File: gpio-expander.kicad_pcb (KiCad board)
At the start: 2 copper layers, 29.2 x 29.4 mm, 13 parts, among them J1 Conn_01x06, J2 Conn_02x07_Odd_Even, J3 Conn_02x04_Odd_Even, U1 TCA9555DBT

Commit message: Rev 1.2
Signed-off-by: Aaron Williams <aaron.w2@gmail.com>
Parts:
- removed JP1, JP2, JP3: SolderJumper_2_Open, SolderJumper:SolderJumper-2_P1.3mm_Open_TrianglePad1.0x1.5mm
- added SW1: SW_DIP_x06, Buttons_Switches_SMD:SW_DIP_x6_W5.08mm_Slide_Copal_CHS-A, F.Cu at (146.2, 109.2)
- C1: footprint Capacitors_SMD:C_0603_HandSoldering -> Capacitor_SMD:C_0603_1608Metric
- C2, C3, C4: footprint Capacitors_SMD:C_0805_HandSoldering -> Capacitor_SMD:C_0805_2012Metric
- J1: footprint Connector_PinHeader_2.00mm:PinHeader_1x06_P2.00mm_Horizontal -> Pin_Headers:Pin_Header_Angled_1x06_Pitch2.54mm
- RN1, RN2: footprint Resistors_SMD:R_Array_Convex_4x0603 -> Resistor_SMD:R_Array_Convex_4x0603
- moved RN2 4.71 mm to (139.2, 110.6), turned to 270 degrees
- moved C3 1.98 mm to (138.7, 105.2), turned to 180 degrees
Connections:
- RN1 pad 5: +3V3 -> Net-(RN1-Pad5)
- RN1 pad 6: +3V3 -> Net-(RN1-Pad6)
- RN1 pad 7: +3V3 -> Net-(RN1-Pad7)
- RN1 pad 8: +3V3 -> Net-(RN1-Pad8)
- RN2 pad 1: +3V3 -> Net-(RN2-Pad1)
- RN2 pad 2: +3V3 -> /A0
- RN2 pad 3: +3V3 -> /A1
- RN2 pad 4: +3V3 -> /A2
- RN2 pad 5: Net-(RN2-Pad5) -> GND
- RN2 pad 6: /A2 -> GND
- RN2 pad 7: /A1 -> GND
- RN2 pad 8: /A0 -> Net-(RN2-Pad8)
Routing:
- net Net-(RN1-Pad6): track 0.00 -> 13.9 mm, vias 0 -> 2
- net Net-(RN1-Pad7): track 0.00 -> 13.7 mm, vias 0 -> 2
- net Net-(RN1-Pad8): track 0.00 -> 13.1 mm, vias 0 -> 2
- net /A0: track 13.0 -> 23.2 mm, vias 0 -> 2
- net /~INT: track 19.0 -> 27.9 mm, vias 2 -> 1
- net +3V3: track 12.3 -> 5.49 mm
- net /A2: track 24.4 -> 20.1 mm
- net /A1: track 22.0 -> 17.9 mm, vias 0 -> 2
- net GND: track 17.5 -> 14.9 mm, vias 6 -> 3
- net /SCL: track 11.5 -> 12.0 mm
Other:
- board text added: "1"
- board text added: "6"
- board text added: "I2C Address: 0x20-0x27"
- board text added: "Rev 1.2"
- board text added: "SW: 1: INT PU 2: SDA PU 3: SCL PU 4: A2 5: A1 6: A0"
- board text removed: "A0"
- board text removed: "A1"
- board text removed: "A2"

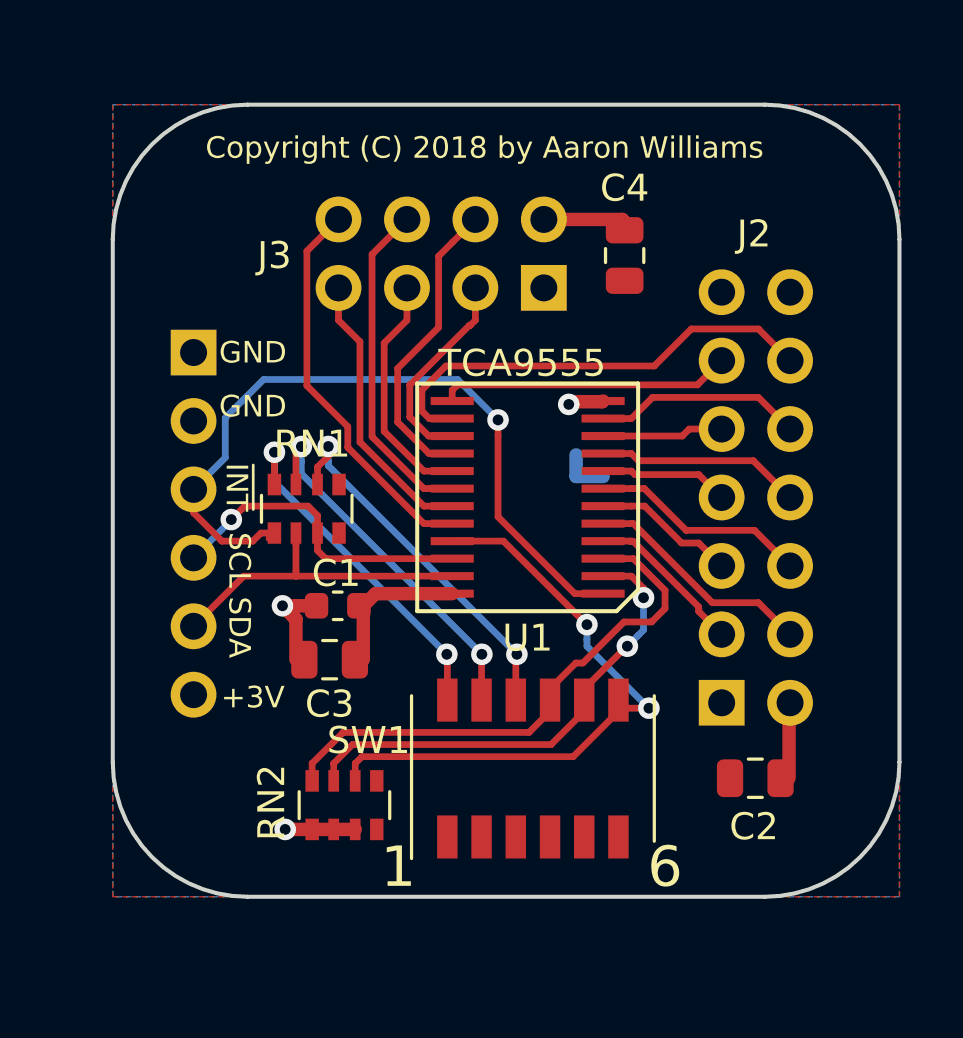
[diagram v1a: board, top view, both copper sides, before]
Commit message: - Added a dip switch for setting the address and termination - Added mounting holes - Changed J1 to a 10-pin connector with all pins duplicated   for stacking - Minor cleanup - Updated README
Signed-off-by: Aaron Williams <aaron.w2@gmail.com>
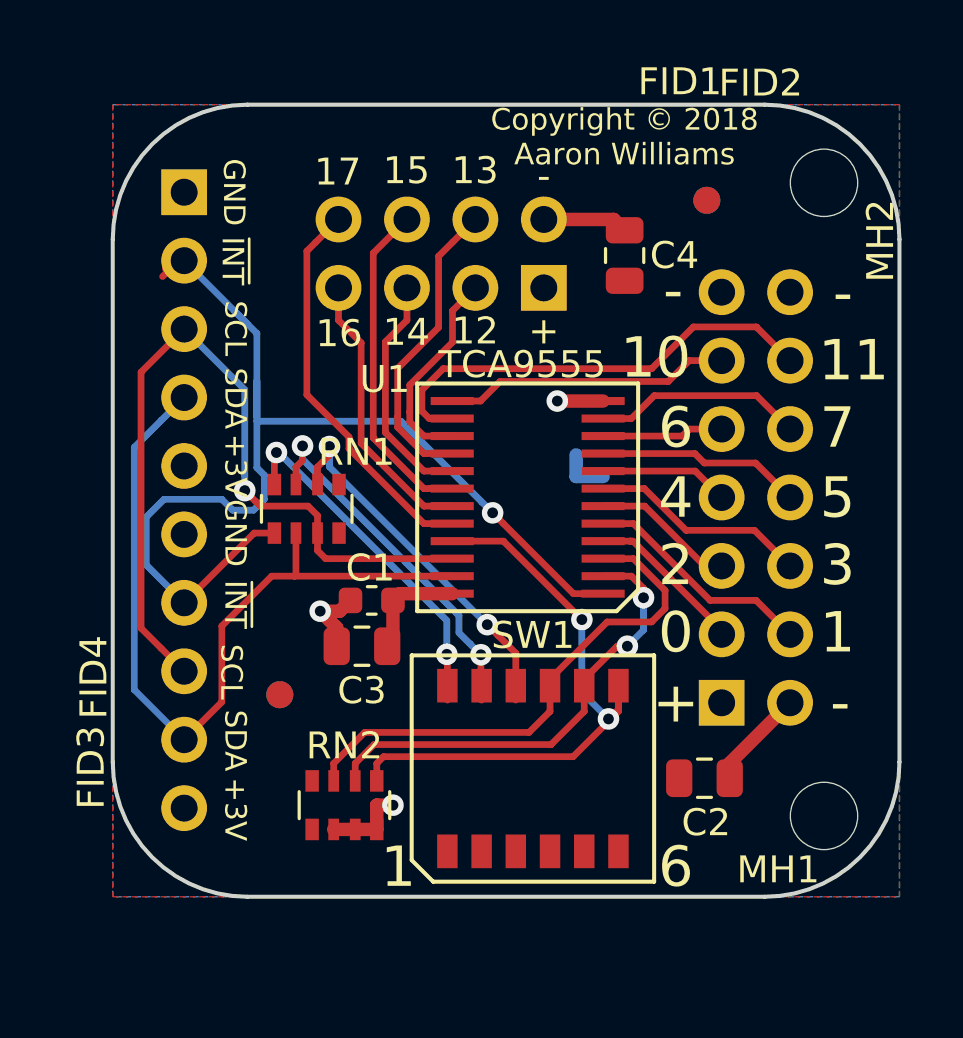
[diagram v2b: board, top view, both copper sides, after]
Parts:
- added FID1: FIDUCIAL_1MM, Fiducial:Fiducial_1mm_Dia_2.54mm_Outer_CopperTop, F.Cu at (152.7, 88.2)
- added FID2: FIDUCIAL_1MM, Fiducial:Fiducial_1mm_Dia_2.54mm_Outer_CopperBottom, F.Cu at (152.7, 88.2)
- added FID3: FIDUCIAL_1MM, Fiducial:Fiducial_1mm_Dia_2.54mm_Outer_CopperBottom, F.Cu at (136.8, 106.5)
- added FID4: FIDUCIAL_1MM, Fiducial:Fiducial_1mm_Dia_2.54mm_Outer_CopperTop, F.Cu at (136.8, 106.5)
- added MH1: MountingHole, MountingHole:MountingHole_2.5mm, F.Cu at (156.9, 111.0)
- added MH2: MountingHole, MountingHole:MountingHole_2.5mm, F.Cu at (157.0, 87.5)
- J1: value Conn_01x06 -> Conn_01x10; footprint Pin_Headers:Pin_Header_Angled_1x06_Pitch2.54mm -> Pin_Headers:Pin_Header_Angled_1x10_Pitch2.54mm
- SW1: footprint Buttons_Switches_SMD:SW_DIP_x6_W5.08mm_Slide_Copal_CHS-A -> Aaron:SW_DIP_SPSTx06_Slide_GrayHill_97C06_W4.5mm_P1.27mm
- moved J1 5.96 mm to (133.2, 87.8)
- moved C2 1.89 mm to (152.6, 109.6)
- moved C3 1.30 mm to (139.8, 104.7)
- moved C1 1.28 mm to (140.2, 103.0)
- turned SW1 to 0 degrees
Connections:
- net Net-(RN1-Pad6) renamed /SDA_PU
- net Net-(RN1-Pad7) renamed /SCL_PU
- net Net-(RN1-Pad8) renamed /~INT_PU
- J1 pad 2: GND -> /~INT
- J1 pad 3: /~INT -> /SCL
- J1 pad 4: /SCL -> /SDA
- J1 pad 5: /SDA -> +3V3
- J1 pad 6: +3V3 -> GND
- RN2 pad 1: Net-(RN2-Pad1) -> /A0
- RN2 pad 2: /A0 -> /A1
- RN2 pad 3: /A1 -> /A2
- RN2 pad 4: /A2 -> Net-(RN2-Pad4)
- RN2 pad 5: GND -> Net-(RN2-Pad5)
- RN2 pad 8: Net-(RN2-Pad8) -> GND
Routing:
- net /SCL: track 12.0 -> 30.5 mm
- net /SDA: track 12.4 -> 30.0 mm
- net /~INT: track 27.9 -> 43.3 mm
- net GND: track 14.9 -> 16.4 mm
- net +3V3: track 5.49 -> 4.09 mm
- net /A1: track 17.9 -> 17.4 mm
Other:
- board text added: "+"
- board text added: "-"
- board text added: "0"
- board text added: "10"
- board text added: "11"
- board text added: "12"
- board text added: "13"
- board text added: "14"
- board text added: "15"
- board text added: "16"
- board text added: "17"
- board text added: "2"
- board text added: "3"
- board text added: "4"
- board text added: "5"
- board text added: "7"
- board text added: "Copyright © 2018 Aaron Williams"
- board text removed: "Copyright (C) 2018 by Aaron Williams"

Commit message: Fixed solder mask clearance.
Signed-off-by: Aaron Williams <aaron.w2@gmail.com>
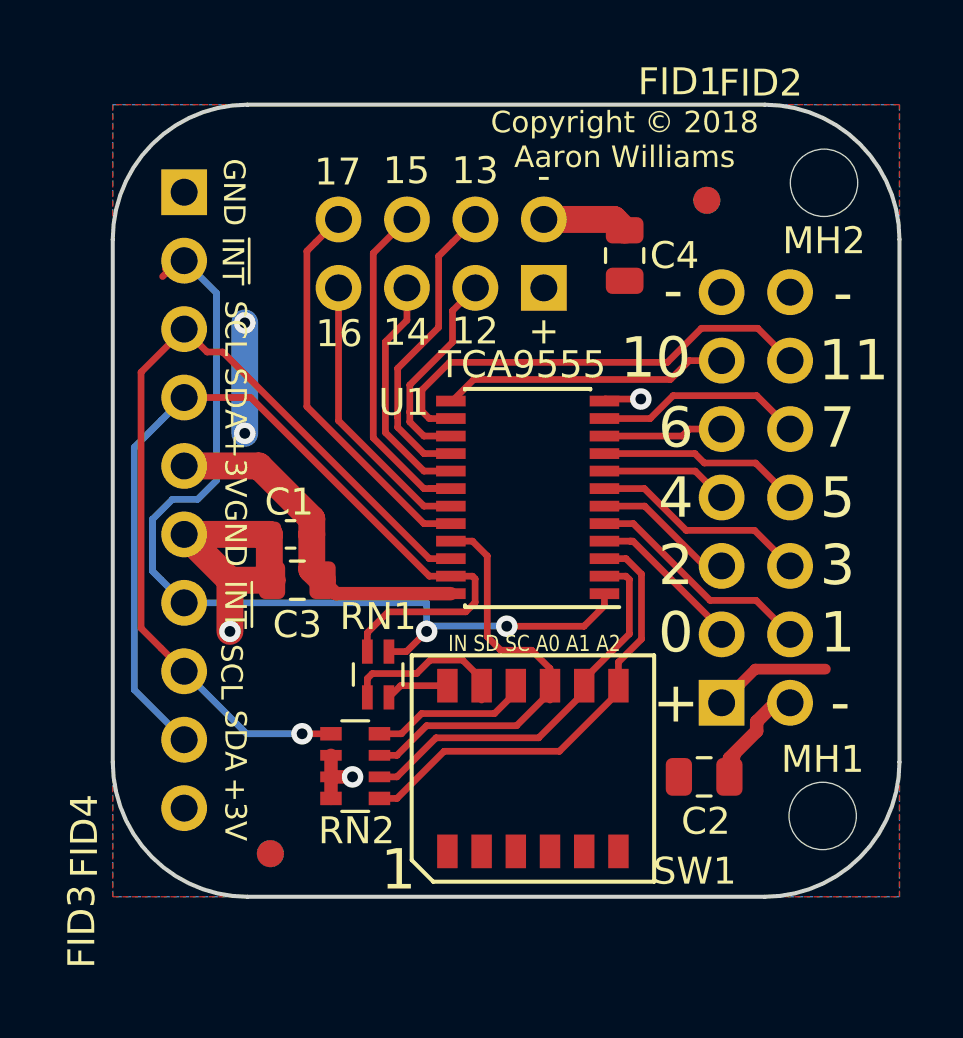
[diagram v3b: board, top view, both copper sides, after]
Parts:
- RN1: value 10k -> R_Pack02; footprint Resistor_SMD:R_Array_Convex_4x0603 -> Resistor_SMD:R_Array_Concave_2x0603
- U1: footprint Housings_SSOP:SOIC-24_5.3x6.2mm_Pitch0.65 -> Housings_SSOP:TSSOP-24_4.4x7.8mm_Pitch0.65mm
- moved RN1 6.70 mm to (140.4, 105.8), turned to 270 degrees
- moved FID3 5.91 mm to (136.4, 112.4)
- moved FID4 5.91 mm to (136.4, 112.4)
- moved C1 3.88 mm to (137.2, 100.5)
- moved C3 3.43 mm to (137.4, 102.2)
- moved RN2 1.50 mm to (139.6, 109.2), turned to 180 degrees
- moved C2 0.05 mm to (152.6, 109.5)
- turned U1 to 180 degrees
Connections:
- RN1 pad 3: /SCL -> /SDA_PU
- RN1 pad 4: Net-(RN1-Pad4) -> /~INT_PU
- RN2 pad 1: /A0 -> /A2
- RN2 pad 3: /A2 -> /A0
- RN2 pad 4: Net-(RN2-Pad4) -> /SCL_PU
- RN2 pad 5: Net-(RN2-Pad5) -> /SCL
- SW1 pad 10: /SDA_PU -> /SCL_PU
- SW1 pad 11: /SCL_PU -> /SDA_PU
- SW1 pad 7: /A0 -> /A2
- SW1 pad 9: /A2 -> /A0
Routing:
- net +3V3: track 4.09 -> 21.4 mm, vias 0 -> 2
- net /~INT_PU: track 13.1 -> 2.35 mm, vias 2 -> 0
- net /SDA_PU: track 13.9 -> 5.80 mm, vias 2 -> 0
- net /SCL_PU: track 13.7 -> 5.94 mm, vias 2 -> 0
- net /A0: track 22.9 -> 16.2 mm, vias 2 -> 0
- net /~INT: track 43.3 -> 36.8 mm, vias 1 -> 2
- net GND: track 16.4 -> 22.1 mm
- net /SDA: track 30.0 -> 33.9 mm
- net /SCL: track 30.5 -> 33.9 mm
- net /A2: track 19.9 -> 16.9 mm
- net /A1: track 17.4 -> 14.8 mm, vias 2 -> 0
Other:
- rule pad_to_mask_clearance: 0.2 -> 0.0508
- board text added: "1.65-6V I2C GPIO Expander"
- board text added: "IN SD SC A0 A1 A2"
- board text added: "Rev 1.3"
- board text added: "Switch SW1: 1: INT PU 2: SDA PU 3: SCL PU 4: A0 5: A1 6: A2"
- board text removed: "3V I2C GPIO Expander"
- board text removed: "Rev 1.2"
- board text removed: "SW: 1: INT PU 2: SDA PU 3: SCL PU 4: A2 5: A1 6: A0"

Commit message: Fixed the footprint to not use a git library.
Signed-off-by: Aaron Williams <aaron.w2@gmail.com>
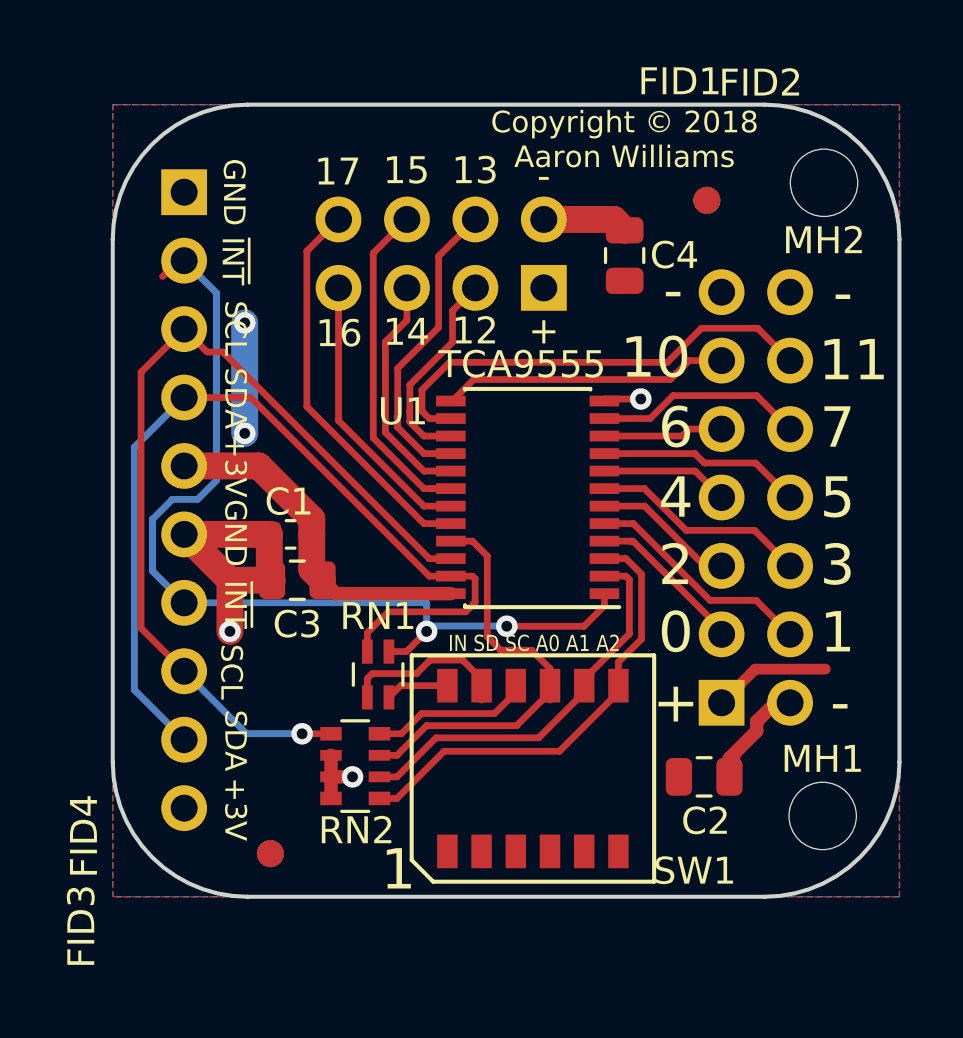
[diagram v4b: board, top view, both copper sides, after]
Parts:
- U1: footprint Housings_SSOP:TSSOP-24_4.4x7.8mm_Pitch0.65mm -> Package_SO:TSSOP-24_4.4x7.8mm_P0.65mm

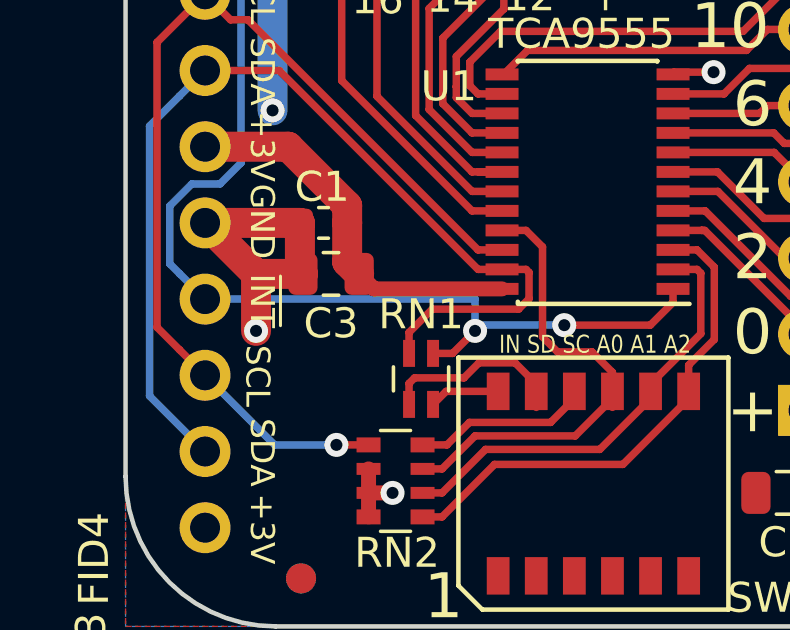
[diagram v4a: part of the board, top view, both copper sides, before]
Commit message: Minor change.  Made trace 45 degree instead of 90 degrees.
Signed-off-by: Aaron Williams <aaron.w2@gmail.com>
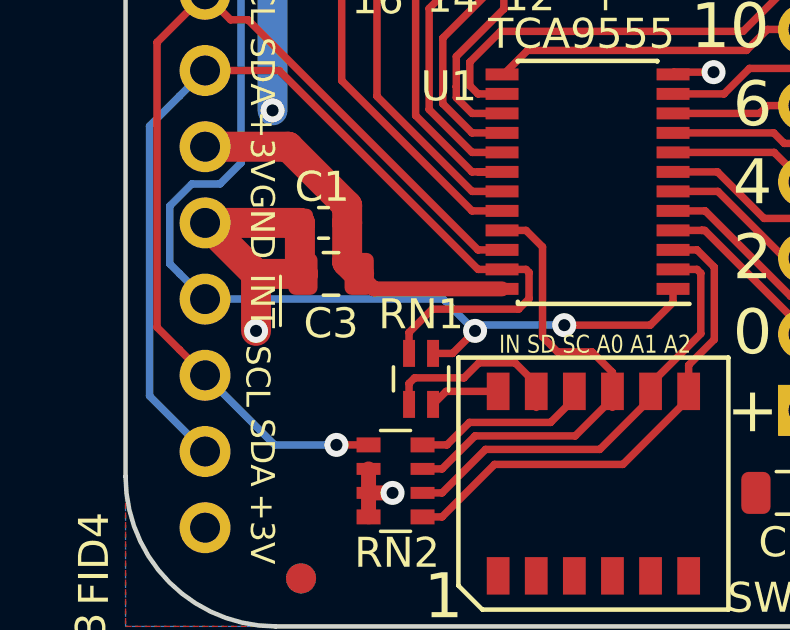
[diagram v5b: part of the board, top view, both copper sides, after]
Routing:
- net /~INT: track 36.8 -> 36.1 mm
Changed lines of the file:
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@@
   (segment (start 140.85 104.9) (end 141.5 104.9) (width 0.25) (layer F.Cu) (net 19) (status 10))
   (via (at 142.25 104.15) (size 0.8) (drill 0.4) (layers F.Cu B.Cu) (net 19))
-  (segment (start 142.25 104.15) (end 142.25 103.09) (width 0.25) (layer B.Cu) (net 19))
-  (segment (start 133.25 103.09) (end 142.25 103.09) (width 0.25) (layer B.Cu) (net 19) (status 10))
   (segment (start 145.216156 103.95) (end 145.22501 103.958854) (width 0.25) (layer B.Cu) (net 19))
   (segment (start 142.25 103.95) (end 145.216156 103.95) (width 0.25) (layer B.Cu) (net 19))
+  (segment (start 141.19 103.09) (end 133.25 103.09) (width 0.25) (layer B.Cu) (net 19))
+  (segment (start 142.25 104.15) (end 141.19 103.09) (width 0.25) (layer B.Cu) (net 19))
   (segment (start 133.25 108.17) (end 131.399989 106.319989) (width 0.25) (layer B.Cu) (net 20) (status 10))
   (segment (start 132.400001 96.319999) (end 133.25 95.47) (width 0.25) (layer B.Cu) (net 20) (status 30))
